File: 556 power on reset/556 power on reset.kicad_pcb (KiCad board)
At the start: 2 copper layers, 32.4 x 22.2 mm, 15 parts, among them J1 Conn_01x04_Socket, Q1 2N7002, U1 NA556

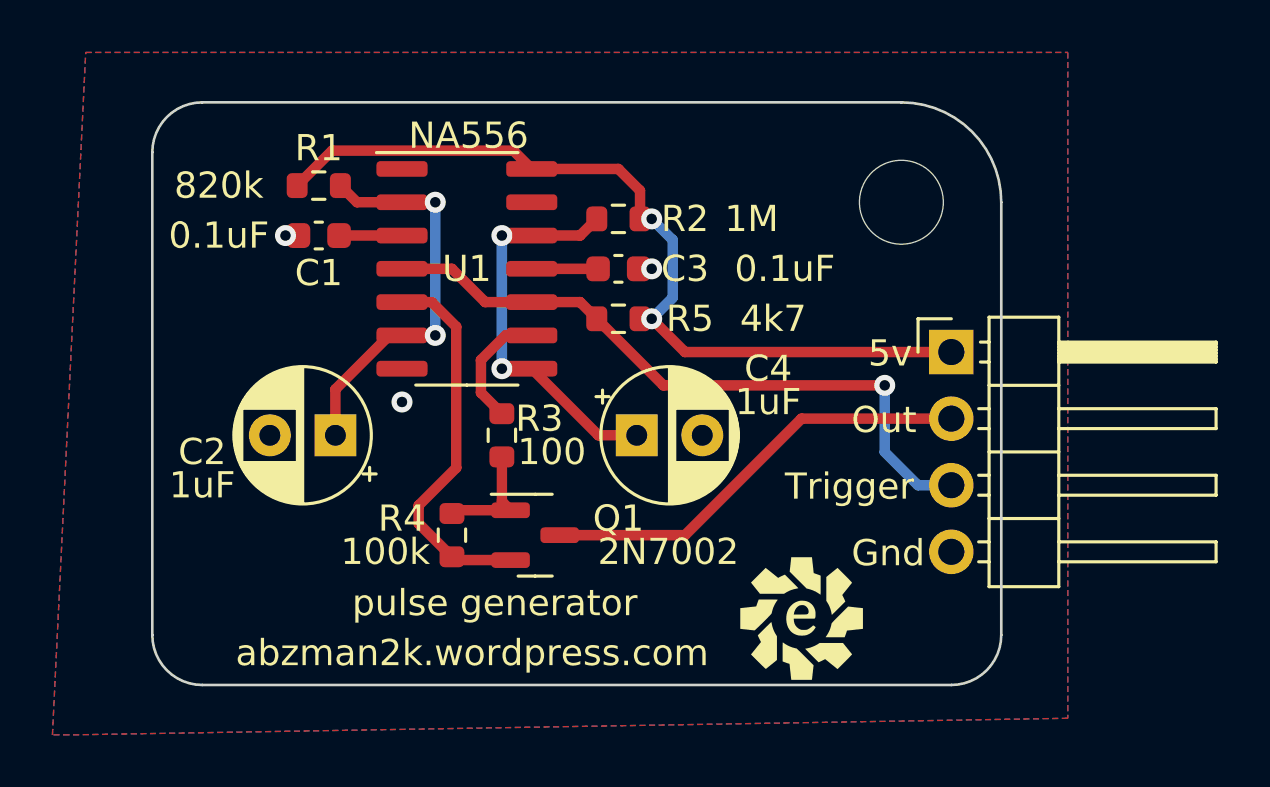
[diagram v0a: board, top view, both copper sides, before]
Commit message: update for bigger capacitors
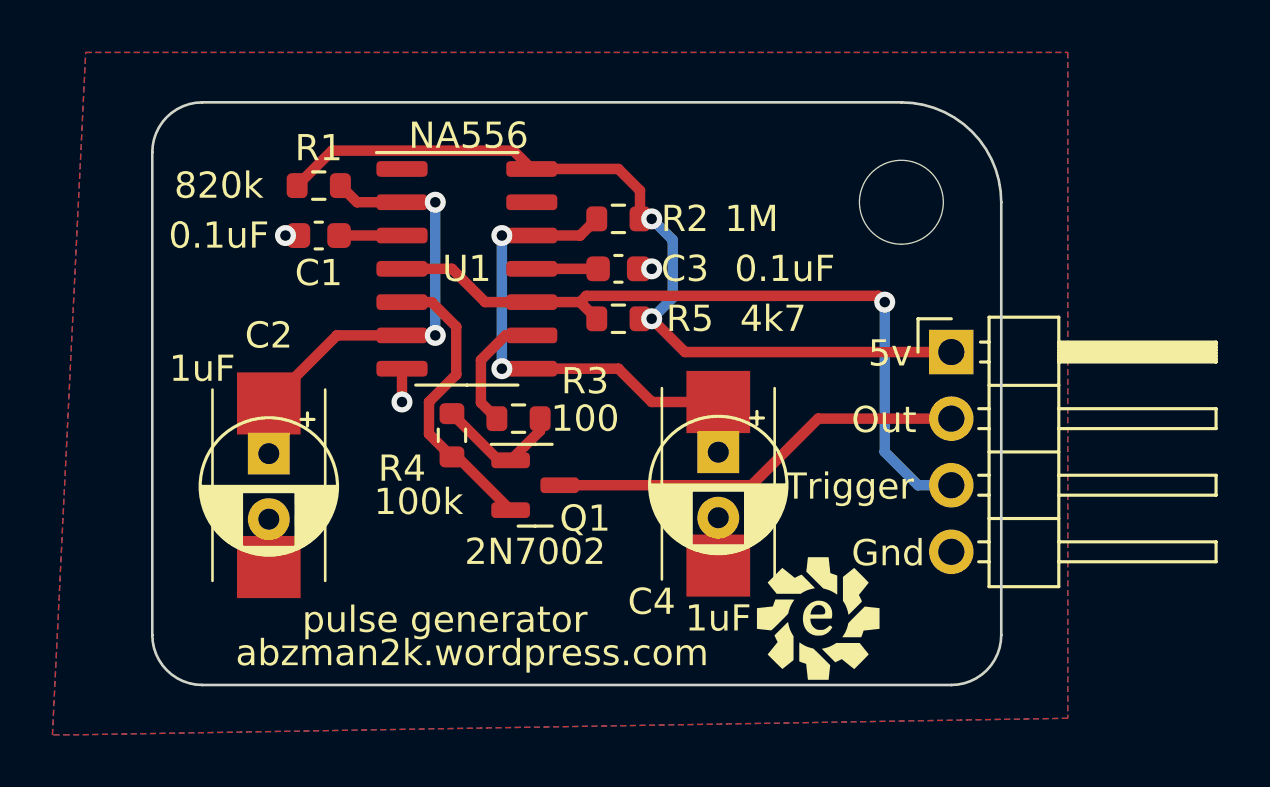
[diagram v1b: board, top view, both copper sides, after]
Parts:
- added C5: 1uF, Evan's parts:V type tantalum, F.Cu at (170.2, 106.0)
- added C6: 1uF, Evan's parts:V type tantalum, F.Cu at (153.0, 106.0)
- moved R4 3.81 mm to (160.0, 104.1)
- moved C4 3.18 mm to (170.2, 104.8), turned to -90 degrees
- moved C2 2.63 mm to (153.0, 104.8), turned to -90 degrees
- moved Q1 1.91 mm to (163.2, 106.0)
- moved R3 0.90 mm to (162.6, 103.5), turned to 0 degrees
- moved G*** 0.64 mm to (174.0, 111.1)
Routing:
- net Net-(Q1-S): track 14.6 -> 11.3 mm
- net Net-(J1-Pin_3): track 25.9 -> 28.8 mm
- net Net-(U1B-THR): track 15.2 -> 17.7 mm
- net GND: track 0.00 -> 1.27 mm
- net Net-(U1A-THR): track 15.4 -> 16.4 mm
- net Net-(J1-Pin_2): track 16.8 -> 16.0 mm
- net Net-(Q1-G): track 4.46 -> 5.03 mm
